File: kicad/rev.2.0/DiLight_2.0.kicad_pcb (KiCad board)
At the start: 2 copper layers, 30.7 x 30.5 mm, 21 parts, among them J1 12V IN, J2 LED strip, J3 Sensor, J4 Touch, J5 ST Link V3, Q1 AP4435C, Q2 AO3400A, U1 AMS1117-3.3, U2 STM32G031G8Ux

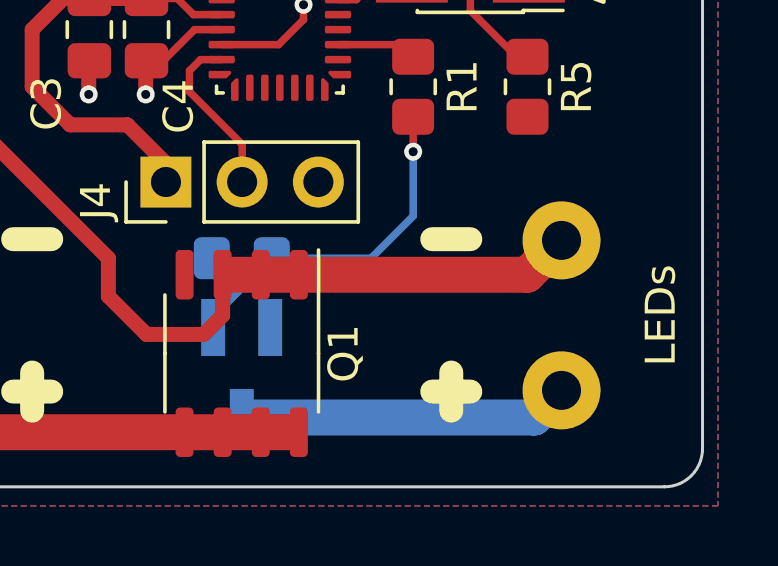
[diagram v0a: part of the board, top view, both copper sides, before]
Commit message: PCB silkscreen +/- marks positions fixed. Manual on/off still works if the range sensor is not initialized
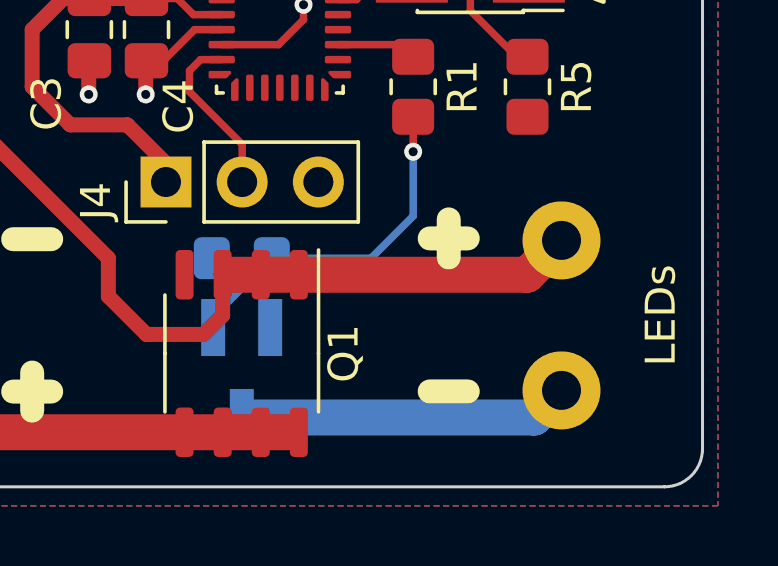
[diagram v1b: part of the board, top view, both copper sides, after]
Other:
- board text added: "DiLight rev. 2.0a"
- board text removed: "DiLight rev. 2.0"
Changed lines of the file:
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@@
     )
   )
-  (gr_line (start 40.005 38.1) (end 40.005 39.37) (layer "B.SilkS") (width 0.8))
-  (gr_line (start 40.64 43.815) (end 39.37 43.815) (layer "B.SilkS") (width 0.8))
+  (gr_line (start 40.005 43.175) (end 40.005 44.445) (layer "B.SilkS") (width 0.8))
+  (gr_line (start 40.695 38.81) (end 39.425 38.81) (layer "B.SilkS") (width 0.8))
   (gr_line (start 31.115 38.1) (end 31.115 39.37) (layer "B.SilkS") (width 0.8))
   (gr_line (start 31.115 43.18) (end 31.115 44.45) (layer "B.SilkS") (width 0.8))
-  (gr_line (start 40.005 43.18) (end 40.005 44.45) (layer "B.SilkS") (width 0.8))
+  (gr_line (start 40.06 38.175) (end 40.06 39.445) (layer "B.SilkS") (width 0.8))
   (gr_line (start 30.48 43.815) (end 31.75 43.815) (layer "B.SilkS") (width 0.8))
   (gr_line (start 25.12 20.02) (end 46.02 20.02) (layer "B.SilkS") (width 0.15))
@@
       (xy 47.62 30.22)
     ) (layer "F.SilkS") (width 0.15) (fill solid))
-  (gr_line (start 41.91 38.735) (end 43.18 38.735) (layer "F.SilkS") (width 0.8))
+  (gr_line (start 41.825 43.81) (end 43.095 43.81) (layer "F.SilkS") (width 0.8))
   (gr_circle (center 34.22 29.32) (end 34.32 29.32) (layer "F.SilkS") (width 0.15) (fill solid))
-  (gr_line (start 42.545 43.18) (end 42.545 44.45) (layer "F.SilkS") (width 0.8))
+  (gr_line (start 42.46 38.075) (end 42.46 39.345) (layer "F.SilkS") (width 0.8))
   (gr_line (start 27.94 38.735) (end 29.21 38.735) (layer "F.SilkS") (width 0.8))
   (gr_line (start 28.575 43.18) (end 28.575 44.45) (layer "F.SilkS") (width 0.8))
-  (gr_line (start 43.18 43.815) (end 41.91 43.815) (layer "F.SilkS") (width 0.8))
+  (gr_line (start 43.095 38.71) (end 41.825 38.71) (layer "F.SilkS") (width 0.8))
   (gr_arc (start 21.49 46.99) (mid 20.591974 46.618026) (end 20.22 45.72) (layer "Edge.Cuts") (width 0.1))
   (gr_line (start 21.49 46.99) (end 49.65 46.99) (layer "Edge.Cuts") (width 0.1))
@@
     (effects (font (size 1 1) (thickness 0.15)) (justify mirror))
   )
-  (gr_text "DiLight\nrev. 2.0" (at 35.56 33.655) (layer "B.SilkS")
+  (gr_text "DiLight\nrev. 2.0a" (at 35.56 33.655) (layer "B.SilkS")
     (effects (font (size 1 1) (thickness 0.15)) (justify mirror))
   )
